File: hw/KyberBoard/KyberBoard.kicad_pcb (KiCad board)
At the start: 4 copper layers, 60.7 x 27.2 mm, 78 parts, among them Q1 STL120N4F6AG, Q2 SIS413DN-T1-GE3, Q3 SSM3K337R, Q4 STL76DN4LF7AG, Q5 SSM3K337R, Q6 SSM3K337R, Q7 SSM3K337R, U1 STM32L051K8Tx, U2 VNHD7008AY, U3 AZ1117IH-3.3TRG1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

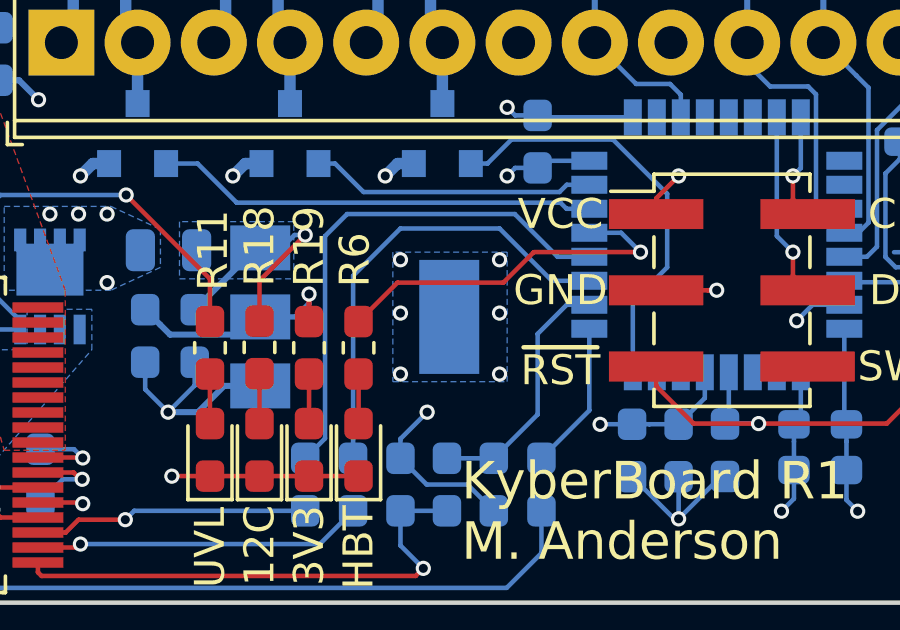
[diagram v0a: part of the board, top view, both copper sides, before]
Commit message: Completed BOM; board sent to fab house
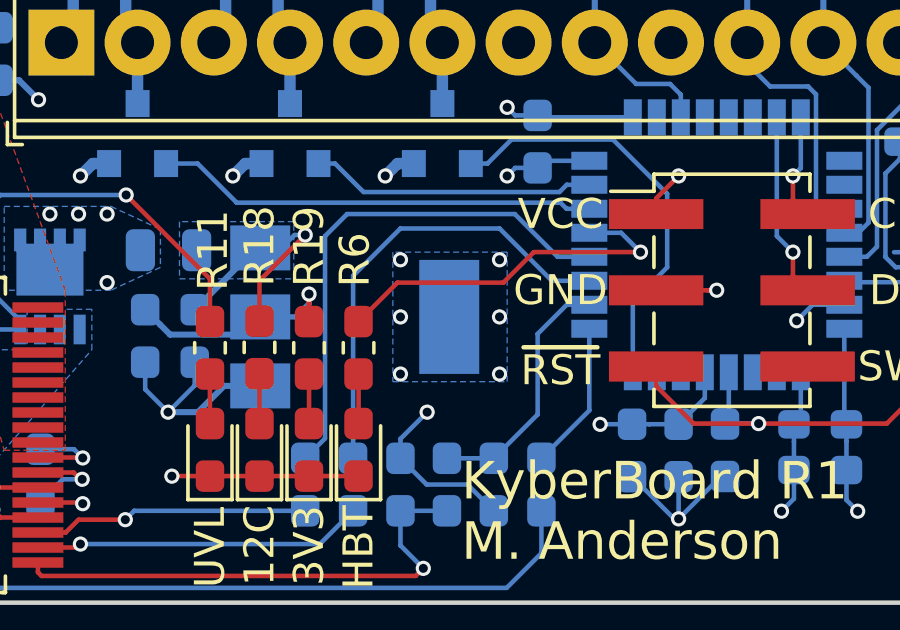
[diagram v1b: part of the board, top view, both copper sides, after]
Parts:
- 12 (x2), 3.3 (x2): value 0 -> RC1005J000CS
- ?: value NUCLEO144ZE-STLINK -> 0015910060
- ?: value SW -> TL3342F160QG/TR
- C1: value 33n -> CC0603KRX7R7BB333
- C10, C11, C9: value 10n -> RM188R72A103KA01J
- C12, C3: value 10u -> GRM188R61E106KA73D
- C13: value 22u -> GRM188R60J226MEA0J
- C15, C17, C18, C2, C4, C5, C7, C8: value 100n -> CC0603KRX7R7BB104
- C16: value 4u7 -> CC0603ZRY5V6BB475
- C19: value 1u -> CC0603KRX7R7BB105
- C6: value 200u -> UWT1E331MNL1GS
- D13, D14, D15: value BZT585B3V6T -> BZT585B3V6T-7
- R1, R10, R19, R2, R20, R3, R6: value 1k -> CRCW06031K00JNTA
- R11, R9: value 0 -> CRCW06030000Z0EBC
- R12, R13, R18, R4: value 10k -> CRCW060310K0JNTA
- R5: value 1k5 -> CRCW06031K50JNTA
- R8: value 1k -> CRCW060310K0JNTA
- U1: value STM32L051K8Tx -> STM32L051K8T6
- U2: value VNHD7008AY -> VNHD7008AYTR
- U4: value MMA8452Q -> MMA8452QT

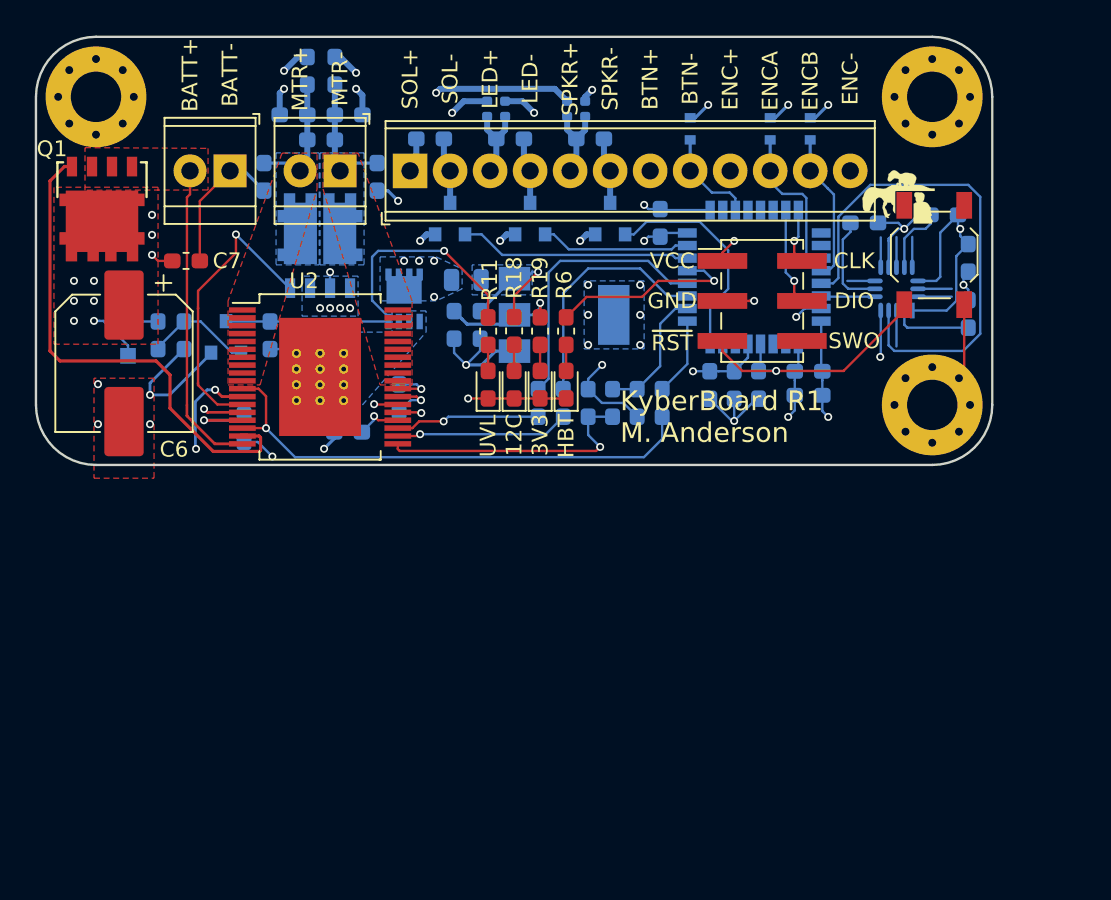
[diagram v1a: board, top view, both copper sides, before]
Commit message: drawing cleanup & pdfs
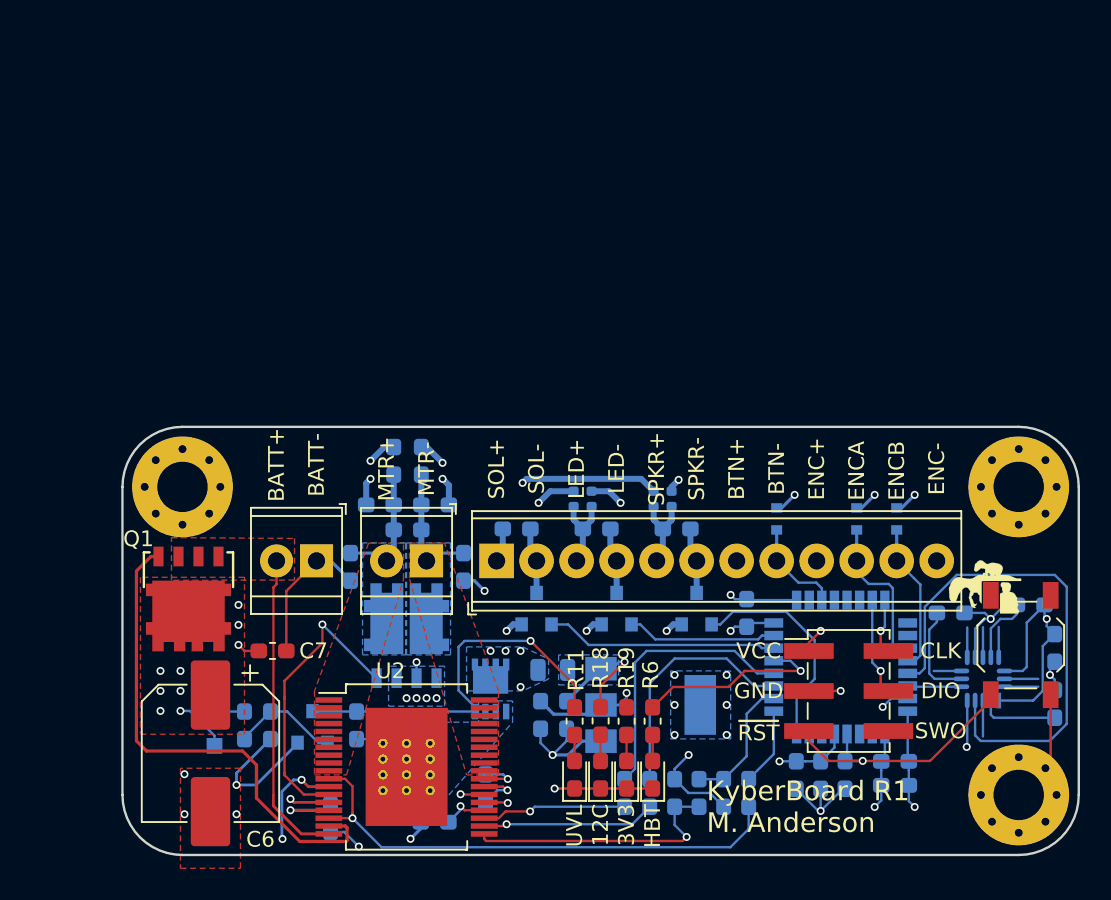
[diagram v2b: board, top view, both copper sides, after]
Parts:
- removed the 12 at (150.1, 67.8)
- removed the 12 at (145.0, 67.8)
- removed the 3.3 at (151.2, 67.8)
- removed the 3.3 at (146.1, 67.8)
- removed the ? at (120.1, 67.1)
- removed the ? at (173.2, 67.1)
- removed the ? at (173.2, 86.6)
- removed the ? at (128.7, 71.8)
- removed the ? at (135.6, 71.8)
- added 12: RC1005J000CS, Resistor_SMD:R_0402_1005Metric, B.Cu at (155.5, 92.6)
- added 12: RC1005J000CS, Resistor_SMD:R_0402_1005Metric, B.Cu at (150.5, 92.6)
- added 3.3: RC1005J000CS, Resistor_SMD:R_0402_1005Metric, B.Cu at (156.7, 92.6)
- added 3.3: RC1005J000CS, Resistor_SMD:R_0402_1005Metric, B.Cu at (151.6, 92.6)
- added ?: MountingHole_Pad, MountingHole:MountingHole_3.2mm_M3_Pad_Via, F.Cu at (125.6, 91.8)
- added ?: MountingHole_Pad, MountingHole:MountingHole_3.2mm_M3_Pad_Via, F.Cu at (178.7, 91.8)
- added ?: MountingHole_Pad, MountingHole:MountingHole_3.2mm_M3_Pad_Via, F.Cu at (178.7, 111.4)
- added ?: 282834-2, TerminalBlock_TE-Connectivity:TerminalBlock_TE_282834-2_1x02_P2.54mm_Horizontal, F.Cu at (134.1, 96.5)
- added ?: 282834-2, TerminalBlock_TE-Connectivity:TerminalBlock_TE_282834-2_1x02_P2.54mm_Horizontal, F.Cu at (141.1, 96.5)
- moved 12C 25.4 mm to (152.2, 110.1)
- moved ? 25.4 mm to (145.6, 96.5)
- moved ? 25.4 mm to (167.9, 104.8)
- moved ? 25.4 mm to (178.8, 101.9)
- moved C1 25.4 mm to (160.0, 111.2)
- moved C10 25.4 mm to (136.3, 96.9)
- moved C11 25.4 mm to (143.5, 96.9)
- moved C19 25.4 mm to (166.1, 110.1)
- moved C2 25.4 mm to (167.7, 110.1)
- moved C7 25.4 mm to (131.3, 102.2)
- moved D13 25.4 mm to (163.4, 93.8)
- moved D14 25.4 mm to (168.4, 93.8)
- moved D15 25.4 mm to (171.0, 93.8)
- moved D4 25.4 mm to (138.2, 93.0)
- moved D5 25.4 mm to (141.7, 93.0)
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
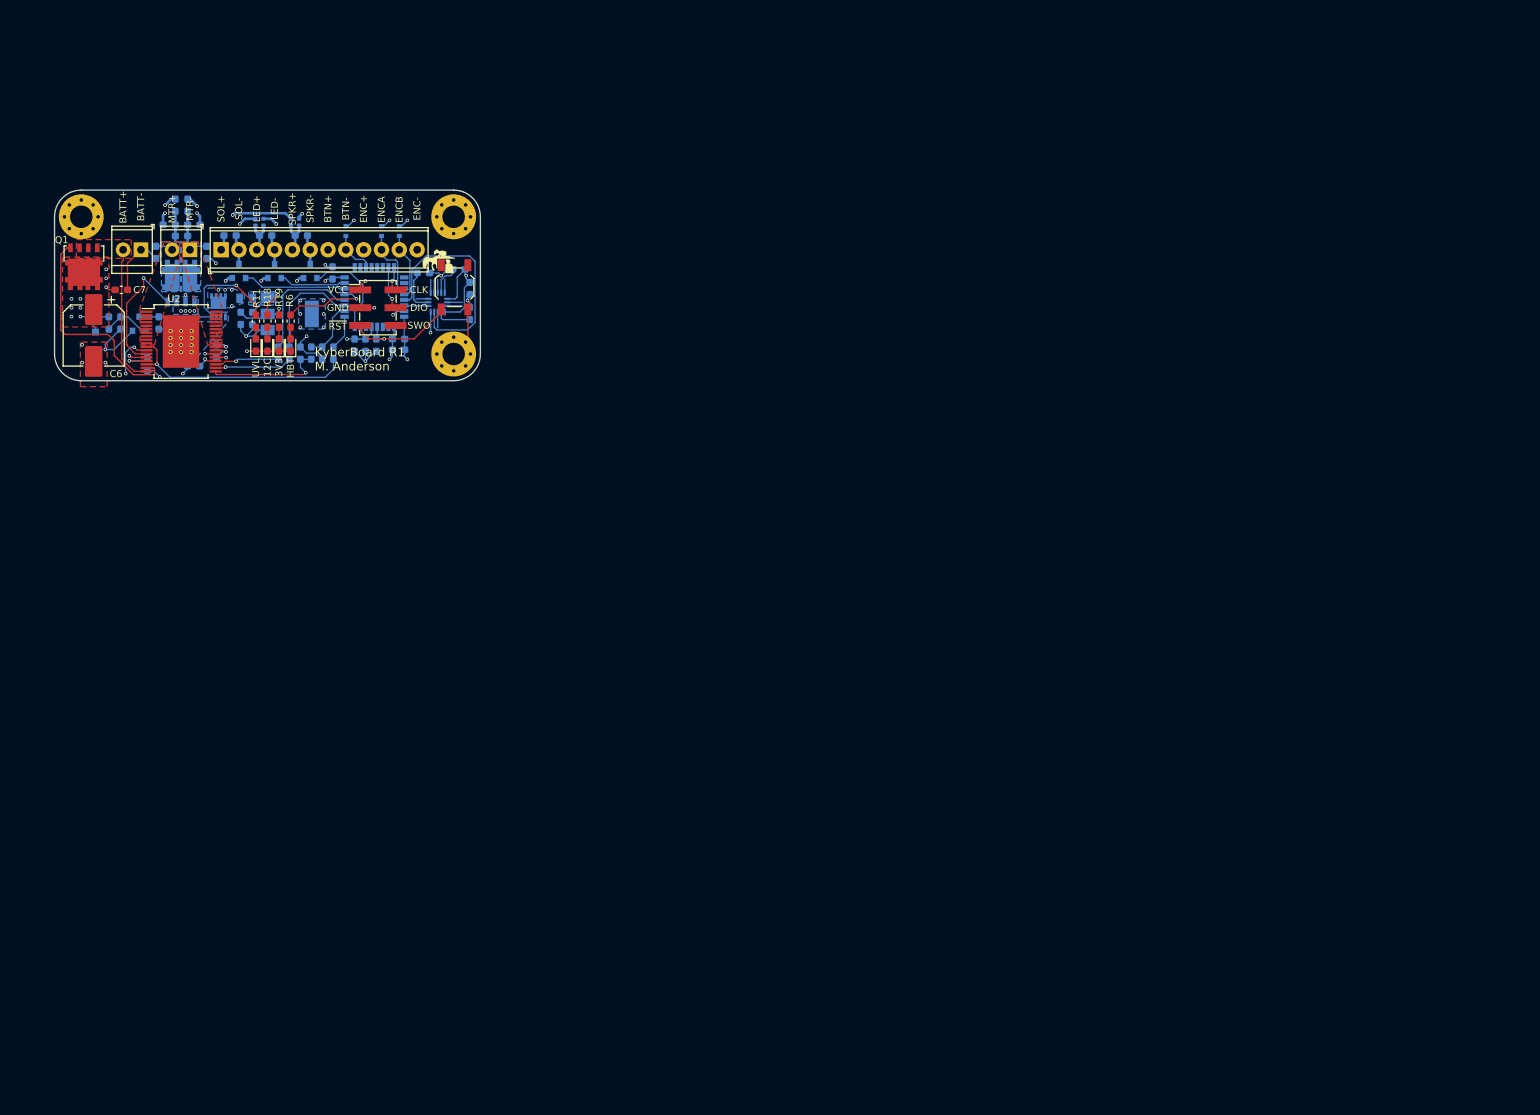
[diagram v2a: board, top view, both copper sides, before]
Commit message: PCB Bring-Up Day 1 Revisions
- Touched up undervoltage cutout circuit
    - Stronger PMOS pull-up (10kOhms was not working; replaced with 1k & called good)
    - 10kOhms LED current-limiting resistor
- Corrected minor schematic discrepancies from PCB
    - undervoltage indicator circuit was correct in PCB but not schematic
- Changed mounting holes from M3 to M2.5 (Raspberry Pi size)
- Found that identifiers can be made invisible
    - now mounting holes have identifiers that do not appear on silkscreen
    - similar logic for LED indicators and jumpers
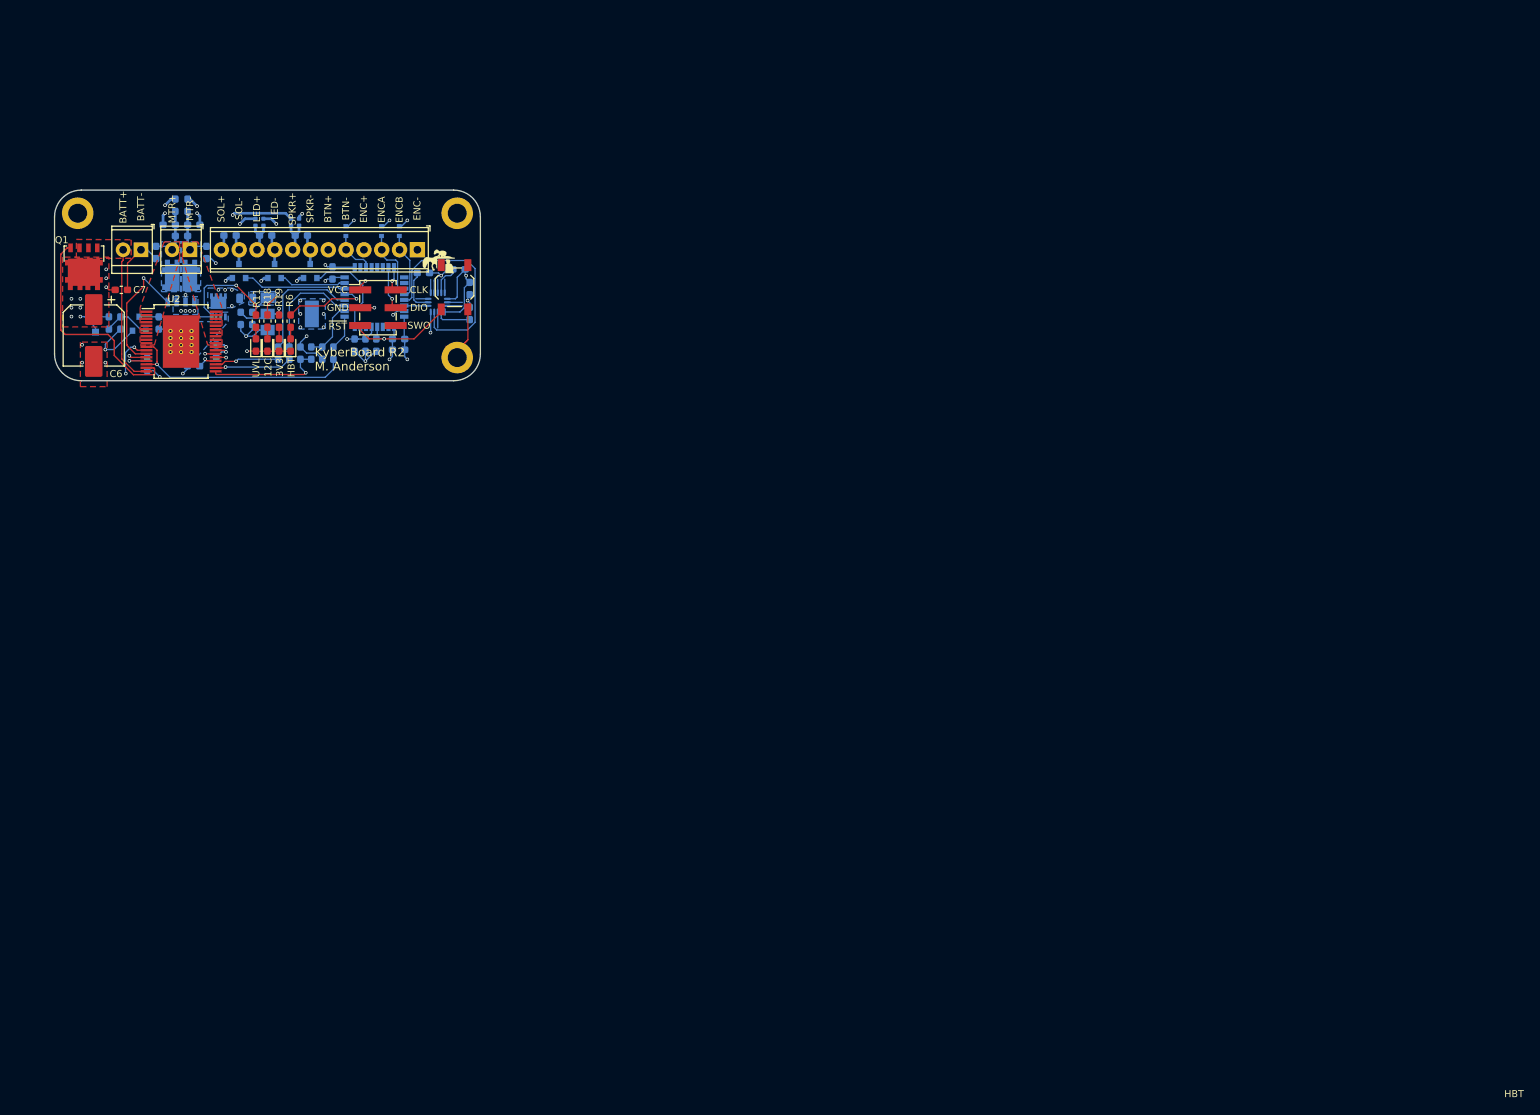
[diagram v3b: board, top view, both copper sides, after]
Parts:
- removed the ? at (145.6, 96.5)
- removed the ? at (125.6, 91.8)
- removed the ? at (178.7, 91.8)
- removed the ? at (178.7, 111.4)
- added ?: , , F.Cu at (153.4, 116.8)
- added H1: MountingHole_Pad, MountingHole:MountingHole_2.7mm_M2.5_ISO7380_Pad, F.Cu at (125.1, 91.3)
- added H3: MountingHole_Pad, MountingHole:MountingHole_2.7mm_M2.5_ISO7380_Pad, F.Cu at (179.2, 91.3)
- added H4: MountingHole_Pad, MountingHole:MountingHole_2.7mm_M2.5_ISO7380_Pad, F.Cu at (179.2, 111.9)
- added J3: OSTVN12A150, TerminalBlock_Phoenix:TerminalBlock_Phoenix_MPT-0,5-12-2.54_1x12_P2.54mm_Horizontal, F.Cu at (173.5, 96.5)
- C1: value CC0603KRX7R7BB333 -> 33n
- C10, C11, C9: value RM188R72A103KA01J -> 10n
- C12, C3: value GRM188R61E106KA73D -> 10u
- C13: value GRM188R60J226MEA0J -> 22u
- C15, C17, C18, C2, C4, C5, C7, C8: value CC0603KRX7R7BB104 -> 100n
- C16: value CC0603ZRY5V6BB475 -> 4u7
- C19: value CC0603KRX7R7BB105 -> 1u
- C6: value UWT1E331MNL1GS -> 200u
- D13, D14, D15: value BZT585B3V6T-7 -> BZT585B3V6T
- J4: renamed from ?; value 0015910060 -> 15910060
- Q5, Q6, Q7: value SSM3K337R -> SSM3K337R,LF
- R1, R10, R19, R2, R20, R3, R6: value CRCW06031K00JNTA -> 1k
- R11: value CRCW06030000Z0EBC -> 10k
- R12, R13, R18, R4: value CRCW060310K0JNTA -> 10k
- R14, R16: renamed from 12; value RC1005J000CS -> 0
- R15, R17: renamed from 3.3; value RC1005J000CS -> 0
- R5: value CRCW06031K50JNTA -> 1k5
- R8: value CRCW060310K0JNTA -> 1k
- R9: value CRCW06030000Z0EBC -> 0
- U2: value VNHD7008AYTR -> VNHD7008AY
- U4: footprint MMA8542:MMA8452Q -> MMA8452:MMA8452Q
- gave numbers to parts that had none: 3
- renumbered HBT to D1, 12C to D10, 3V3 to D11, UVL to D3
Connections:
- net /hbridge/VCC renamed /V_UNSAFE
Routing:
- net GND: track 132.6 -> 110.9 mm
- net /LED+: track 8.78 -> 5.91 mm
- net /SPKR+: track 7.66 -> 5.51 mm
- net /acc/SCL: track 32.6 -> 31.5 mm
- net +3V3: track 49.2 -> 48.3 mm
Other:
- board text added: "12"
- board text added: "12C"
- board text added: "3.3"
- board text added: "3V3"
- board text added: "HBT"
- board text added: "KyberBoard R2 M. Anderson"
- board text added: "UVL"
- board text removed: "KyberBoard R1 M. Anderson"
